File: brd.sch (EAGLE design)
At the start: 16 parts, among them IC1 OP27Z, X1 BNC-H, X2 BNC-H, X3 BNC-H, X4 BNC-H

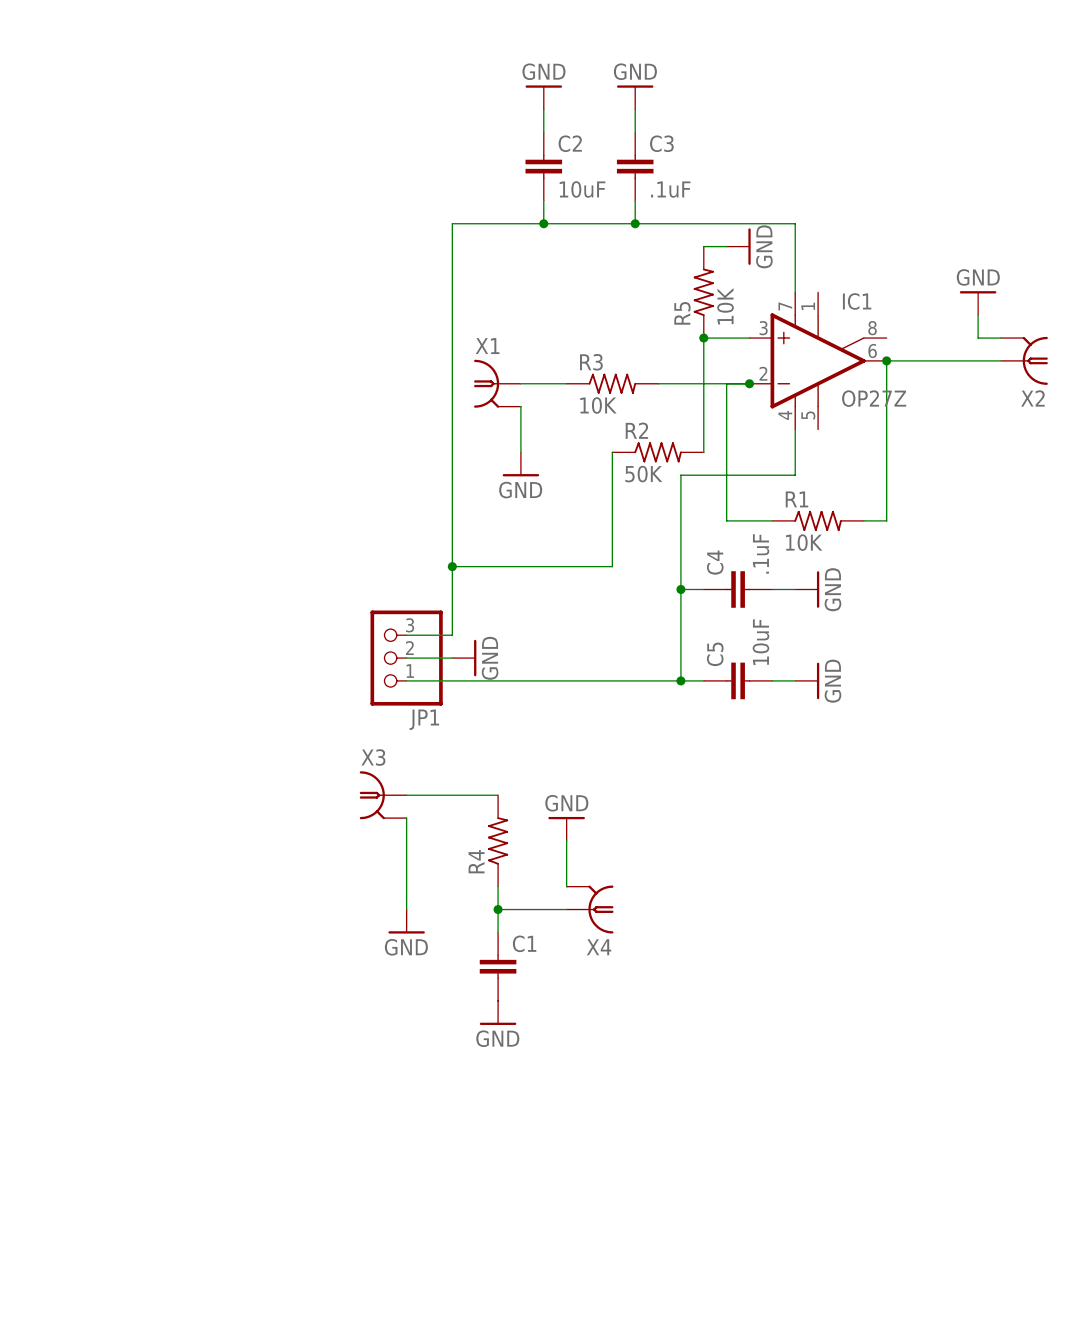
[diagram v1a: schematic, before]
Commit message: added switches
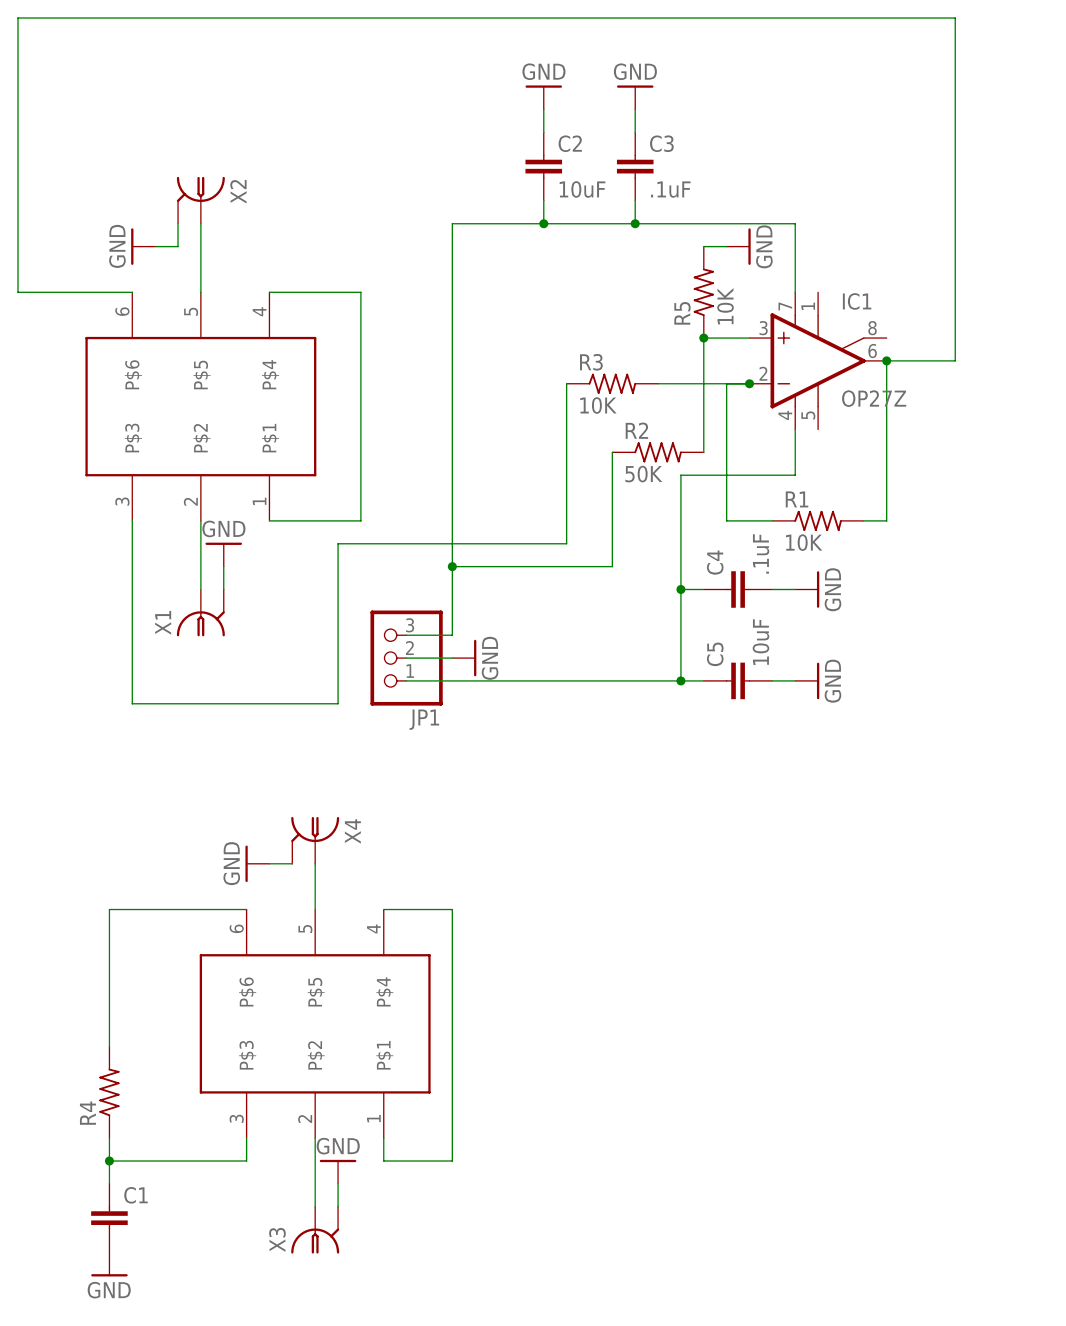
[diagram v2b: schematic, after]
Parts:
- added U$1, U$2: DP3T-TOGGLE, switch-jqi:DP3T-TOGGLE
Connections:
- new net N$10: U$2.P$1, U$2.P$4
- new net N$12: U$1.P$5, X2.1
- new net N$14: R3.1, U$1.P$3
- new net N$15: U$1.P$1, U$1.P$4
- new net N$16: R4.2, U$2.P$6
- new net N$4: U$2.P$2, X3.1
- net N$2: now also U$1.P$6; no longer X2.1
- net N$5: now also U$2.P$5, X4.1; no longer R4.2, X3.1
- net N$6: now also U$1.P$2; no longer R3.1
- net N$8: now also U$2.P$3; no longer X4.1
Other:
- moved on the sheet: C1, R4, X1, X2, X3, X4
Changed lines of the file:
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@@
 <part name="GND11" library="supply1" deviceset="GND" device=""/>
 <part name="R5" library="resistor" deviceset="R-US_" device="0204/2V" value="10K"/>
+<part name="U$1" library="switch-jqi" deviceset="DP3T-TOGGLE" device=""/>
+<part name="U$2" library="switch-jqi" deviceset="DP3T-TOGGLE" device=""/>
 </parts>
 <sheets>
@@
 <instance part="IC1" gate="A" x="15.24" y="106.68"/>
 <instance part="GND1" gate="1" x="7.62" y="119.38" rot="R90"/>
-<instance part="X1" gate="G$1" x="-20.32" y="104.14"/>
-<instance part="X2" gate="G$1" x="38.1" y="106.68" rot="R180"/>
-<instance part="X3" gate="G$1" x="-33.02" y="58.42"/>
-<instance part="X4" gate="G$1" x="-10.16" y="45.72" rot="R180"/>
+<instance part="X1" gate="G$1" x="-53.34" y="78.74" rot="R90"/>
+<instance part="X2" gate="G$1" x="-53.34" y="124.46" rot="R270"/>
+<instance part="X3" gate="G$1" x="-40.64" y="10.16" rot="R90"/>
+<instance part="X4" gate="G$1" x="-40.64" y="53.34" rot="R270"/>
 <instance part="JP1" gate="A" x="-33.02" y="73.66" rot="R180"/>
 <instance part="GND2" gate="1" x="-22.86" y="73.66" rot="R90"/>
-<instance part="GND3" gate="1" x="-17.78" y="93.98"/>
+<instance part="GND3" gate="1" x="-50.8" y="86.36" rot="R180"/>
 <instance part="R1" gate="G$1" x="15.24" y="88.9"/>
 <instance part="R2" gate="G$1" x="-2.54" y="96.52"/>
 <instance part="R3" gate="G$1" x="-7.62" y="104.14"/>
-<instance part="GND4" gate="1" x="33.02" y="114.3" rot="R180"/>
-<instance part="GND5" gate="1" x="-30.48" y="43.18"/>
-<instance part="GND6" gate="1" x="-12.7" y="55.88" rot="R180"/>
-<instance part="R4" gate="G$1" x="-20.32" y="53.34" rot="R90"/>
-<instance part="C1" gate="G$1" x="-20.32" y="40.64"/>
+<instance part="GND4" gate="1" x="-60.96" y="119.38" rot="R270"/>
+<instance part="GND5" gate="1" x="-38.1" y="17.78" rot="R180"/>
+<instance part="GND6" gate="1" x="-48.26" y="50.8" rot="R270"/>
+<instance part="R4" gate="G$1" x="-63.5" y="25.4" rot="R90"/>
+<instance part="C1" gate="G$1" x="-63.5" y="12.7"/>
 <instance part="C2" gate="G$1" x="-15.24" y="129.54"/>
 <instance part="C3" gate="G$1" x="-5.08" y="129.54"/>
 <instance part="C4" gate="G$1" x="5.08" y="81.28" rot="R90"/>
 <instance part="C5" gate="G$1" x="5.08" y="71.12" rot="R90"/>
-<instance part="GND7" gate="1" x="-20.32" y="33.02"/>
+<instance part="GND7" gate="1" x="-63.5" y="5.08"/>
 <instance part="GND8" gate="1" x="-15.24" y="137.16" rot="R180"/>
 <instance part="GND9" gate="1" x="-5.08" y="137.16" rot="R180"/>
@@
 <instance part="GND11" gate="1" x="15.24" y="71.12" rot="R90"/>
 <instance part="R5" gate="G$1" x="2.54" y="114.3" rot="R90"/>
+<instance part="U$1" gate="G$1" x="-53.34" y="101.6" rot="R90"/>
+<instance part="U$2" gate="G$1" x="-40.64" y="33.02" rot="R90"/>
 </instances>
 <busses>
@@
 <pinref part="X1" gate="G$1" pin="2"/>
 <pinref part="GND3" gate="1" pin="GND"/>
-<wire x1="-17.78" y1="101.6" x2="-17.78" y2="96.52" width="0.1524" layer="91"/>
-</segment>
-<segment>
-<pinref part="GND4" gate="1" pin="GND"/>
-<wire x1="33.02" y1="111.76" x2="33.02" y2="109.22" width="0.1524" layer="91"/>
-<pinref part="X2" gate="G$1" pin="2"/>
-<wire x1="35.56" y1="109.22" x2="33.02" y2="109.22" width="0.1524" layer="91"/>
+<wire x1="-50.8" y1="83.82" x2="-50.8" y2="81.28" width="0.1524" layer="91"/>
 </segment>
 <segment>
 <pinref part="X3" gate="G$1" pin="2"/>
 <pinref part="GND5" gate="1" pin="GND"/>
-<wire x1="-30.48" y1="55.88" x2="-30.48" y2="45.72" width="0.1524" layer="91"/>
+<wire x1="-38.1" y1="12.7" x2="-38.1" y2="15.24" width="0.1524" layer="91"/>
 </segment>
 <segment>
 <pinref part="X4" gate="G$1" pin="2"/>
 <pinref part="GND6" gate="1" pin="GND"/>
-<wire x1="-12.7" y1="48.26" x2="-12.7" y2="53.34" width="0.1524" layer="91"/>
+<wire x1="-43.18" y1="50.8" x2="-45.72" y2="50.8" width="0.1524" layer="91"/>
 </segment>
 <segment>
@@
 <pinref part="GND1" gate="1" pin="GND"/>
 <wire x1="2.54" y1="119.38" x2="5.08" y2="119.38" width="0.1524" layer="91"/>
+</segment>
+<segment>
+<pinref part="GND4" gate="1" pin="GND"/>
+<pinref part="X2" gate="G$1" pin="2"/>
+<wire x1="-58.42" y1="119.38" x2="-55.88" y2="119.38" width="0.1524" layer="91"/>
+<wire x1="-55.88" y1="119.38" x2="-55.88" y2="121.92" width="0.1524" layer="91"/>
 </segment>
 </net>
@@
 <wire x1="22.86" y1="88.9" x2="22.86" y2="106.68" width="0.1524" layer="91"/>
 <pinref part="R1" gate="G$1" pin="2"/>
-<pinref part="X2" gate="G$1" pin="1"/>
-<wire x1="22.86" y1="106.68" x2="35.56" y2="106.68" width="0.1524" layer="91"/>
+<wire x1="22.86" y1="106.68" x2="30.48" y2="106.68" width="0.1524" layer="91"/>
+<wire x1="30.48" y1="106.68" x2="30.48" y2="144.78" width="0.1524" layer="91"/>
 <junction x="22.86" y="106.68"/>
+<wire x1="30.48" y1="144.78" x2="-73.66" y2="144.78" width="0.1524" layer="91"/>
+<pinref part="U$1" gate="G$1" pin="P$6"/>
+<wire x1="-60.96" y1="114.3" x2="-73.66" y2="114.3" width="0.1524" layer="91"/>
+<wire x1="-73.66" y1="114.3" x2="-73.66" y2="144.78" width="0.1524" layer="91"/>
 </segment>
 </net>
@@
 </segment>
 </net>
-<net name="N$5" class="0">
-<segment>
-<pinref part="X3" gate="G$1" pin="1"/>
-<pinref part="R4" gate="G$1" pin="2"/>
-<wire x1="-30.48" y1="58.42" x2="-20.32" y2="58.42" width="0.1524" layer="91"/>
-</segment>
-</net>
 <net name="N$8" class="0">
 <segment>
 <pinref part="R4" gate="G$1" pin="1"/>
 <pinref part="C1" gate="G$1" pin="1"/>
-<wire x1="-20.32" y1="48.26" x2="-20.32" y2="45.72" width="0.1524" layer="91"/>
-<wire x1="-20.32" y1="45.72" x2="-20.32" y2="43.18" width="0.1524" layer="91"/>
-<wire x1="-20.32" y1="45.72" x2="-12.7" y2="45.72" width="0.1524" layer="91"/>
-<junction x="-20.32" y="45.72"/>
-<pinref part="X4" gate="G$1" pin="1"/>
+<wire x1="-63.5" y1="20.32" x2="-63.5" y2="17.78" width="0.1524" layer="91"/>
+<pinref part="U$2" gate="G$1" pin="P$3"/>
+<wire x1="-63.5" y1="17.78" x2="-63.5" y2="15.24" width="0.1524" layer="91"/>
+<wire x1="-63.5" y1="17.78" x2="-48.26" y2="17.78" width="0.1524" layer="91"/>
+<wire x1="-48.26" y1="17.78" x2="-48.26" y2="20.32" width="0.1524" layer="91"/>
+<junction x="-63.5" y="17.78"/>
 </segment>
 </net>
@@
 </segment>
 </net>
+<net name="N$5" class="0">
+<segment>
+<pinref part="U$2" gate="G$1" pin="P$5"/>
+<pinref part="X4" gate="G$1" pin="1"/>
+<wire x1="-40.64" y1="45.72" x2="-40.64" y2="50.8" width="0.1524" layer="91"/>
+</segment>
+</net>
+<net name="N$4" class="0">
+<segment>
+<pinref part="X3" gate="G$1" pin="1"/>
+<pinref part="U$2" gate="G$1" pin="P$2"/>
+<wire x1="-40.64" y1="12.7" x2="-40.64" y2="20.32" width="0.1524" layer="91"/>
+</segment>
+</net>
+<net name="N$12" class="0">
+<segment>
+<pinref part="X2" gate="G$1" pin="1"/>
+<pinref part="U$1" gate="G$1" pin="P$5"/>
+<wire x1="-53.34" y1="121.92" x2="-53.34" y2="114.3" width="0.1524" layer="91"/>
+</segment>
+</net>
 <net name="N$6" class="0">
 <segment>
 <pinref part="X1" gate="G$1" pin="1"/>
+<pinref part="U$1" gate="G$1" pin="P$2"/>
+<wire x1="-53.34" y1="81.28" x2="-53.34" y2="88.9" width="0.1524" layer="91"/>
+</segment>
+</net>
+<net name="N$14" class="0">
+<segment>
 <pinref part="R3" gate="G$1" pin="1"/>
-<wire x1="-17.78" y1="104.14" x2="-12.7" y2="104.14" width="0.1524" layer="91"/>
-</segment>
-</net>
+<wire x1="-12.7" y1="86.36" x2="-12.7" y2="104.14" width="0.1524" layer="91"/>
+<pinref part="U$1" gate="G$1" pin="P$3"/>
+<wire x1="-60.96" y1="88.9" x2="-60.96" y2="68.58" width="0.1524" layer="91"/>
+<wire x1="-60.96" y1="68.58" x2="-38.1" y2="68.58" width="0.1524" layer="91"/>
+<wire x1="-38.1" y1="68.58" x2="-38.1" y2="86.36" width="0.1524" layer="91"/>
+<wire x1="-38.1" y1="86.36" x2="-12.7" y2="86.36" width="0.1524" layer="91"/>
+</segment>
+</net>
+<net name="N$16" class="0">
+<segment>
+<pinref part="R4" gate="G$1" pin="2"/>
+<pinref part="U$2" gate="G$1" pin="P$6"/>
+<wire x1="-48.26" y1="45.72" x2="-63.5" y2="45.72" width="0.1524" layer="91"/>
+<wire x1="-63.5" y1="45.72" x2="-63.5" y2="30.48" width="0.1524" layer="91"/>
+</segment>
+</net>
+<net name="N$10" class="0">
+<segment>
+<pinref part="U$2" gate="G$1" pin="P$4"/>
+<wire x1="-33.02" y1="45.72" x2="-25.4" y2="45.72" width="0.1524" layer="91"/>
+<wire x1="-25.4" y1="45.72" x2="-25.4" y2="17.78" width="0.1524" layer="91"/>
+<pinref part="U$2" gate="G$1" pin="P$1"/>
+<wire x1="-25.4" y1="17.78" x2="-33.02" y2="17.78" width="0.1524" layer="91"/>
+<wire x1="-33.02" y1="17.78" x2="-33.02" y2="20.32" width="0.1524" layer="91"/>
+</segment>
+</net>
+<net name="N$15" class="0">
+<segment>
+<pinref part="U$1" gate="G$1" pin="P$4"/>
+<wire x1="-45.72" y1="114.3" x2="-35.56" y2="114.3" width="0.1524" layer="91"/>
+<wire x1="-35.56" y1="114.3" x2="-35.56" y2="88.9" width="0.1524" layer="91"/>
+<pinref part="U$1" gate="G$1" pin="P$1"/>
+<wire x1="-35.56" y1="88.9" x2="-45.72" y2="88.9" width="0.1524" layer="91"/>
+</segment>
+</net>
